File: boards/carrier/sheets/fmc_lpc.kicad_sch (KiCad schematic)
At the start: 3 parts, among them J1 FX10A-168P-SV(91)

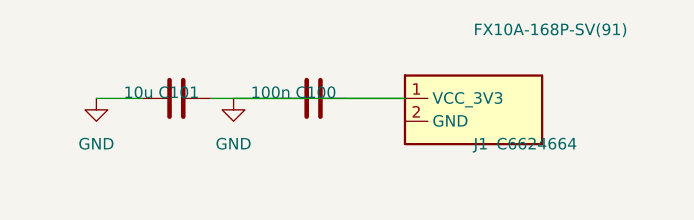
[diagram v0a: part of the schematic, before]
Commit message: Track 4: connector auto-NC + +VIN aliasing fix + +3V3_SC remap + uart_bridge VBUS
Salvaged from stopped agent worktree (a4788480cecd09625). Code-only changes:
* core/layout/connectors.py: auto-NC unused connector pins
* core/layout/_constants.py: drop +VIN → power:+5V aliasing
* core/layout/root.py: explicit PWR_FLAG path for +VIN
* core/model/block.py: IcInstance.external_part_net_remap field
* core/layout/cluster.py: honour remap in resolve_destination_net
* projects/carrier/blocks/usb_pd.py: remap +3V3_SC → +3V3
* projects/carrier/blocks/uart_bridge.py: swap micro-USB for generic header

ERC: 35 → 32 errors (SoM J1/J2/J3 pin_not_connected gone via connector auto-NC).

Co-Authored-By: Claude Opus 4.7 <noreply@anthropic.com>
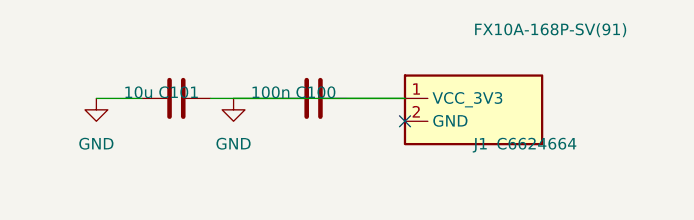
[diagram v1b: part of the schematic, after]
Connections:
- no-connect marks 0 -> 1
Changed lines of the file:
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@@
 		(instances
 			(project "FMC LPC Expansion (VITA 57.1 LPC connector)"
-				(path "/a36bf80b-0e01-480d-934c-128a683fde92"
+				(path "/c798e083-1bae-43bb-ae6c-f9d1340f5d43"
 					(reference "J1")
 					(unit 1)
@@
 		(instances
 			(project "FMC LPC Expansion (VITA 57.1 LPC connector)"
-				(path "/a36bf80b-0e01-480d-934c-128a683fde92"
+				(path "/c798e083-1bae-43bb-ae6c-f9d1340f5d43"
 					(reference "C100")
 					(unit 1)
@@
 		(instances
 			(project "FMC LPC Expansion (VITA 57.1 LPC connector)"
-				(path "/a36bf80b-0e01-480d-934c-128a683fde92"
+				(path "/c798e083-1bae-43bb-ae6c-f9d1340f5d43"
 					(reference "#PWR100")
 					(unit 1)
@@
 		(instances
 			(project "FMC LPC Expansion (VITA 57.1 LPC connector)"
-				(path "/a36bf80b-0e01-480d-934c-128a683fde92"
+				(path "/c798e083-1bae-43bb-ae6c-f9d1340f5d43"
 					(reference "C101")
 					(unit 1)
@@
 		(instances
 			(project "FMC LPC Expansion (VITA 57.1 LPC connector)"
-				(path "/a36bf80b-0e01-480d-934c-128a683fde92"
+				(path "/c798e083-1bae-43bb-ae6c-f9d1340f5d43"
 					(reference "#PWR101")
 					(unit 1)
@@
 		(instances
 			(project "FMC LPC Expansion (VITA 57.1 LPC connector)"
-				(path "/a36bf80b-0e01-480d-934c-128a683fde92"
+				(path "/c798e083-1bae-43bb-ae6c-f9d1340f5d43"
 					(reference "#PWR102")
 					(unit 1)
@@
 		)
 	)
+	(no_connect
+		(at 228.6 38.1)
+	)
 	(sheet_instances
